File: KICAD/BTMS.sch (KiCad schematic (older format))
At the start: 314 parts, among them J1 fan, J10 U1COMMS, J11 U2COMMS, J13 IntBTemp, J14 ctrlTemp, J15 12Vout, J16 12Vin, J17 5Vout, J2 mContactor, J3 Tac, J5 ICSP, J7 5Vout, J9 key, Q1 PSMN5R6-100BS, Q10 PSMN5R6-100BS, Q11 DMN65D8L, Q12 DMN65D8L, Q13 FDN340P, Q14 ZXTP2025FTA, Q15 ZXTP2025FTA, Q16 ZXTP2025FTA, Q18 DMN65D8L, Q2 PSMN5R6-100BS, Q3 PSMN5R6-100BS, Q4 DMN65D8L, Q5 DMN65D8L, Q6 DMN65D8L, Q7 DMN65D8L, Q8 PSMN5R6-100BS, Q9 FDN340P, U1 R-78HB12-0.5, U10 A41AS12VDC, U11 A41AS12VDC, U12 A41AS12VDC, U13 A41AS12VDC, U14 A41AS12VDC, U15 NL17SZ74USG, U2 ACS780xLRTR-050B, U3 UCC27201DDAR, U4 FAN3111ESX, U5 HCPL-3120, U6 L7805CV, U7 LTV-817S, U8 dsPIC30F3011-PT, U9 LM62CIM3/NOPB

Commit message: Updated KICAD custom parts.
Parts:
- U10, U11, U12, U13, U14: symbol a4series:A4series -> BTMS-rescue:A4series-a4series
- U15: symbol nl17sz74usg:NL17SZ74USG -> BTMS-rescue:NL17SZ74USG-nl17sz74usg
- U3: symbol ir2104power:IR2104Power -> BTMS-rescue:IR2104Power-ir2104power
- U8: symbol dspic:dsPIC30F3011-PT -> BTMS-rescue:dsPIC30F3011-PT-dspic
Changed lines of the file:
@@
 Connection ~ 1400 3100
 $Comp
-L ir2104power:IR2104Power U3
+L BTMS-rescue:IR2104Power-ir2104power U3
 U 1 1 5EB473C3
 P 4100 5700
@@
 Connection ~ 13400 8800
 $Comp
-L dspic:dsPIC30F3011-PT U8
+L BTMS-rescue:dsPIC30F3011-PT-dspic U8
 U 1 1 5E12A7C4
 P 13550 7500
@@
 	1650 5400 1650 5750
 $Comp
-L a4series:A4series U10
+L BTMS-rescue:A4series-a4series U10
 U 1 1 5FB8A273
 P 2100 8350
@@
 $EndComp
 $Comp
-L a4series:A4series U11
+L BTMS-rescue:A4series-a4series U11
 U 1 1 5FB8C6D2
 P 2100 9500
@@
 $EndComp
 $Comp
-L a4series:A4series U12
+L BTMS-rescue:A4series-a4series U12
 U 1 1 5FB8DA7B
 P 2100 10700
@@
 $EndComp
 $Comp
-L a4series:A4series U14
+L BTMS-rescue:A4series-a4series U14
 U 1 1 5FB8F1EB
 P 5050 10150
@@
 Connection ~ 5200 9700
 $Comp
-L a4series:A4series U13
+L BTMS-rescue:A4series-a4series U13
 U 1 1 5FB905AA
 P 5050 8600
@@
 	5250 6850 5350 6850
 $Comp
-L nl17sz74usg:NL17SZ74USG U15
+L BTMS-rescue:NL17SZ74USG-nl17sz74usg U15
 U 1 1 6056CB7B
 P 5500 5800

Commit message: Updated parts list. Updated Gerber files. Updated board to reflect schematic. Tweaked some parts of the schematic.
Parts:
- C110, C13, C15, C16, C17, C18, C19, C2, C20, C21, C22, C23, C36, C65, C75, C76, C8: DK_Detail_Page (none) -> https://www.digikey.com/en/products/detail/panasonic-electr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; Digi-Key_PN (none) -> PCF1126CT-ND
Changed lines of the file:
@@
 F 2 "Capacitors_SMD:C_0603" H 5038 3800 50  0001 C CNN
 F 3 "~" H 5000 3950 50  0001 C CNN
-F 4 "" H 5000 3950 50  0001 C CNN "DK_Detail_Page"
-F 5 "" H 5000 3950 50  0001 C CNN "Digi-Key_PN"
+F 4 "https://www.digikey.com/en/products/detail/panasonic-electronic-components/ECP-U1C104MA5/285446?s=N4IgTCBcDaIIxzANgCIGkBKBaAcikAugL5A" H 5000 3950 50  0001 C CNN "DK_Detail_Page"
+F 5 "PCF1126CT-ND" H 5000 3950 50  0001 C CNN "Digi-Key_PN"
 	1    5000 3950
 	1    0    0    -1
@@
 F 2 "Capacitors_SMD:C_0603" H 12638 5900 50  0001 C CNN
 F 3 "~" H 12600 6050 50  0001 C CNN
-F 4 "" H 12600 6050 50  0001 C CNN "DK_Detail_Page"
-F 5 "" H 12600 6050 50  0001 C CNN "Digi-Key_PN"
+F 4 "https://www.digikey.com/en/products/detail/panasonic-electronic-components/ECP-U1C104MA5/285446?s=N4IgTCBcDaIIxzANgCIGkBKBaAcikAugL5A" H 12600 6050 50  0001 C CNN "DK_Detail_Page"
+F 5 "PCF1126CT-ND" H 12600 6050 50  0001 C CNN "Digi-Key_PN"
 	1    12600 6050
 	1    0    0    -1
@@
 F 2 "Capacitors_SMD:C_0603" H 12888 5900 50  0001 C CNN
 F 3 "~" H 12850 6050 50  0001 C CNN
-F 4 "" H 12850 6050 50  0001 C CNN "DK_Detail_Page"
-F 5 "" H 12850 6050 50  0001 C CNN "Digi-Key_PN"
+F 4 "https://www.digikey.com/en/products/detail/panasonic-electronic-components/ECP-U1C104MA5/285446?s=N4IgTCBcDaIIxzANgCIGkBKBaAcikAugL5A" H 12850 6050 50  0001 C CNN "DK_Detail_Page"
+F 5 "PCF1126CT-ND" H 12850 6050 50  0001 C CNN "Digi-Key_PN"
 	1    12850 6050
 	1    0    0    -1
@@
 F 2 "Capacitors_SMD:C_0603" H 12388 5900 50  0001 C CNN
 F 3 "~" H 12350 6050 50  0001 C CNN
-F 4 "" H 12350 6050 50  0001 C CNN "DK_Detail_Page"
-F 5 "" H 12350 6050 50  0001 C CNN "Digi-Key_PN"
+F 4 "https://www.digikey.com/en/products/detail/panasonic-electronic-components/ECP-U1C104MA5/285446?s=N4IgTCBcDaIIxzANgCIGkBKBaAcikAugL5A" H 12350 6050 50  0001 C CNN "DK_Detail_Page"
+F 5 "PCF1126CT-ND" H 12350 6050 50  0001 C CNN "Digi-Key_PN"
 	1    12350 6050
 	1    0    0    -1
@@
 F 2 "Capacitors_SMD:C_0603" H 12138 5900 50  0001 C CNN
 F 3 "~" H 12100 6050 50  0001 C CNN
-F 4 "" H 12100 6050 50  0001 C CNN "DK_Detail_Page"
-F 5 "" H 12100 6050 50  0001 C CNN "Digi-Key_PN"
+F 4 "https://www.digikey.com/en/products/detail/panasonic-electronic-components/ECP-U1C104MA5/285446?s=N4IgTCBcDaIIxzANgCIGkBKBaAcikAugL5A" H 12100 6050 50  0001 C CNN "DK_Detail_Page"
+F 5 "PCF1126CT-ND" H 12100 6050 50  0001 C CNN "Digi-Key_PN"
 	1    12100 6050
 	1    0    0    -1
@@
 F 2 "Capacitors_SMD:C_0603" H 11088 8150 50  0001 C CNN
 F 3 "~" H 11050 8300 50  0001 C CNN
-F 4 "" H 11050 8300 50  0001 C CNN "DK_Detail_Page"
-F 5 "" H 11050 8300 50  0001 C CNN "Digi-Key_PN"
+F 4 "https://www.digikey.com/en/products/detail/panasonic-electronic-components/ECP-U1C104MA5/285446?s=N4IgTCBcDaIIxzANgCIGkBKBaAcikAugL5A" H 11050 8300 50  0001 C CNN "DK_Detail_Page"
+F 5 "PCF1126CT-ND" H 11050 8300 50  0001 C CNN "Digi-Key_PN"
 	1    11050 8300
 	1    0    0    -1
@@
 F 2 "Capacitors_SMD:C_0603" H 10588 1550 50  0001 C CNN
 F 3 "~" H 10550 1700 50  0001 C CNN
-F 4 "" H 10550 1700 50  0001 C CNN "DK_Detail_Page"
-F 5 "" H 10550 1700 50  0001 C CNN "Digi-Key_PN"
+F 4 "https://www.digikey.com/en/products/detail/panasonic-electronic-components/ECP-U1C104MA5/285446?s=N4IgTCBcDaIIxzANgCIGkBKBaAcikAugL5A" H 10550 1700 50  0001 C CNN "DK_Detail_Page"
+F 5 "PCF1126CT-ND" H 10550 1700 50  0001 C CNN "Digi-Key_PN"
 	1    10550 1700
 	1    0    0    -1
@@
 F 2 "Capacitors_SMD:C_0603" H 10588 2250 50  0001 C CNN
 F 3 "~" H 10550 2400 50  0001 C CNN
-F 4 "" H 10550 2400 50  0001 C CNN "DK_Detail_Page"
-F 5 "" H 10550 2400 50  0001 C CNN "Digi-Key_PN"
+F 4 "https://www.digikey.com/en/products/detail/panasonic-electronic-components/ECP-U1C104MA5/285446?s=N4IgTCBcDaIIxzANgCIGkBKBaAcikAugL5A" H 10550 2400 50  0001 C CNN "DK_Detail_Page"
+F 5 "PCF1126CT-ND" H 10550 2400 50  0001 C CNN "Digi-Key_PN"
 	1    10550 2400
 	1    0    0    -1
@@
 F 2 "Capacitors_SMD:C_0603" H 7638 1700 50  0001 C CNN
 F 3 "~" H 7600 1850 50  0001 C CNN
-F 4 "" H 7600 1850 50  0001 C CNN "DK_Detail_Page"
-F 5 "" H 7600 1850 50  0001 C CNN "Digi-Key_PN"
+F 4 "https://www.digikey.com/en/products/detail/panasonic-electronic-components/ECP-U1C104MA5/285446?s=N4IgTCBcDaIIxzANgCIGkBKBaAcikAugL5A" H 7600 1850 50  0001 C CNN "DK_Detail_Page"
+F 5 "PCF1126CT-ND" H 7600 1850 50  0001 C CNN "Digi-Key_PN"
 	1    7600 1850
 	1    0    0    -1
@@
 F 2 "Capacitors_SMD:C_0603" H 8288 1700 50  0001 C CNN
 F 3 "~" H 8250 1850 50  0001 C CNN
-F 4 "" H 8250 1850 50  0001 C CNN "DK_Detail_Page"
-F 5 "" H 8250 1850 50  0001 C CNN "Digi-Key_PN"
+F 4 "https://www.digikey.com/en/products/detail/panasonic-electronic-components/ECP-U1C104MA5/285446?s=N4IgTCBcDaIIxzANgCIGkBKBaAcikAugL5A" H 8250 1850 50  0001 C CNN "DK_Detail_Page"
+F 5 "PCF1126CT-ND" H 8250 1850 50  0001 C CNN "Digi-Key_PN"
 	1    8250 1850
 	1    0    0    -1
@@
 F 2 "Capacitors_SMD:C_0603" H 10488 3150 50  0001 C CNN
 F 3 "~" H 10450 3300 50  0001 C CNN
-F 4 "" H 10450 3300 50  0001 C CNN "DK_Detail_Page"
-F 5 "" H 10450 3300 50  0001 C CNN "Digi-Key_PN"
+F 4 "https://www.digikey.com/en/products/detail/panasonic-electronic-components/ECP-U1C104MA5/285446?s=N4IgTCBcDaIIxzANgCIGkBKBaAcikAugL5A" H 10450 3300 50  0001 C CNN "DK_Detail_Page"
+F 5 "PCF1126CT-ND" H 10450 3300 50  0001 C CNN "Digi-Key_PN"
 	1    10450 3300
 	1    0    0    -1
@@
 F 2 "Capacitors_SMD:C_0603" H 10688 1050 50  0001 C CNN
 F 3 "~" H 10650 1200 50  0001 C CNN
-F 4 "" H 10650 1200 50  0001 C CNN "DK_Detail_Page"
-F 5 "" H 10650 1200 50  0001 C CNN "Digi-Key_PN"
+F 4 "https://www.digikey.com/en/products/detail/panasonic-electronic-components/ECP-U1C104MA5/285446?s=N4IgTCBcDaIIxzANgCIGkBKBaAcikAugL5A" H 10650 1200 50  0001 C CNN "DK_Detail_Page"
+F 5 "PCF1126CT-ND" H 10650 1200 50  0001 C CNN "Digi-Key_PN"
 	1    10650 1200
 	1    0    0    -1
@@
 F 2 "Capacitors_SMD:C_0603" H 6838 1050 50  0001 C CNN
 F 3 "~" H 6800 1200 50  0001 C CNN
-F 4 "" H 6800 1200 50  0001 C CNN "DK_Detail_Page"
-F 5 "" H 6800 1200 50  0001 C CNN "Digi-Key_PN"
+F 4 "https://www.digikey.com/en/products/detail/panasonic-electronic-components/ECP-U1C104MA5/285446?s=N4IgTCBcDaIIxzANgCIGkBKBaAcikAugL5A" H 6800 1200 50  0001 C CNN "DK_Detail_Page"
+F 5 "PCF1126CT-ND" H 6800 1200 50  0001 C CNN "Digi-Key_PN"
 	1    6800 1200
 	1    0    0    -1
@@
 F 2 "Capacitors_SMD:C_0603" H 5788 4800 50  0001 C CNN
 F 3 "~" H 5750 4950 50  0001 C CNN
-F 4 "" H 5750 4950 50  0001 C CNN "DK_Detail_Page"
-F 5 "" H 5750 4950 50  0001 C CNN "Digi-Key_PN"
+F 4 "https://www.digikey.com/en/products/detail/panasonic-electronic-components/ECP-U1C104MA5/285446?s=N4IgTCBcDaIIxzANgCIGkBKBaAcikAugL5A" H 5750 4950 50  0001 C CNN "DK_Detail_Page"
+F 5 "PCF1126CT-ND" H 5750 4950 50  0001 C CNN "Digi-Key_PN"
 	1    5750 4950
 	1    0    0    -1
@@
 F 2 "Capacitors_SMD:C_0603" H 4588 4800 50  0001 C CNN
 F 3 "~" H 4550 4950 50  0001 C CNN
-F 4 "" H 4550 4950 50  0001 C CNN "DK_Detail_Page"
-F 5 "" H 4550 4950 50  0001 C CNN "Digi-Key_PN"
+F 4 "https://www.digikey.com/en/products/detail/panasonic-electronic-components/ECP-U1C104MA5/285446?s=N4IgTCBcDaIIxzANgCIGkBKBaAcikAugL5A" H 4550 4950 50  0001 C CNN "DK_Detail_Page"
+F 5 "PCF1126CT-ND" H 4550 4950 50  0001 C CNN "Digi-Key_PN"
 	1    4550 4950
 	1    0    0    -1
@@
 F 2 "Capacitors_SMD:C_0603" H 2788 6500 50  0001 C CNN
 F 3 "~" H 2750 6650 50  0001 C CNN
-F 4 "" H 2750 6650 50  0001 C CNN "DK_Detail_Page"
-F 5 "" H 2750 6650 50  0001 C CNN "Digi-Key_PN"
+F 4 "https://www.digikey.com/en/products/detail/panasonic-electronic-components/ECP-U1C104MA5/285446?s=N4IgTCBcDaIIxzANgCIGkBKBaAcikAugL5A" H 2750 6650 50  0001 C CNN "DK_Detail_Page"
+F 5 "PCF1126CT-ND" H 2750 6650 50  0001 C CNN "Digi-Key_PN"
 	1    2750 6650
 	1    0    0    -1
@@
 F 2 "Capacitors_SMD:C_0603" H 6338 6000 50  0001 C CNN
 F 3 "~" H 6300 6150 50  0001 C CNN
-F 4 "" H 6300 6150 50  0001 C CNN "DK_Detail_Page"
-F 5 "" H 6300 6150 50  0001 C CNN "Digi-Key_PN"
+F 4 "https://www.digikey.com/en/products/detail/panasonic-electronic-components/ECP-U1C104MA5/285446?s=N4IgTCBcDaIIxzANgCIGkBKBaAcikAugL5A" H 6300 6150 50  0001 C CNN "DK_Detail_Page"
+F 5 "PCF1126CT-ND" H 6300 6150 50  0001 C CNN "Digi-Key_PN"
 	1    6300 6150
 	1    0    0    -1

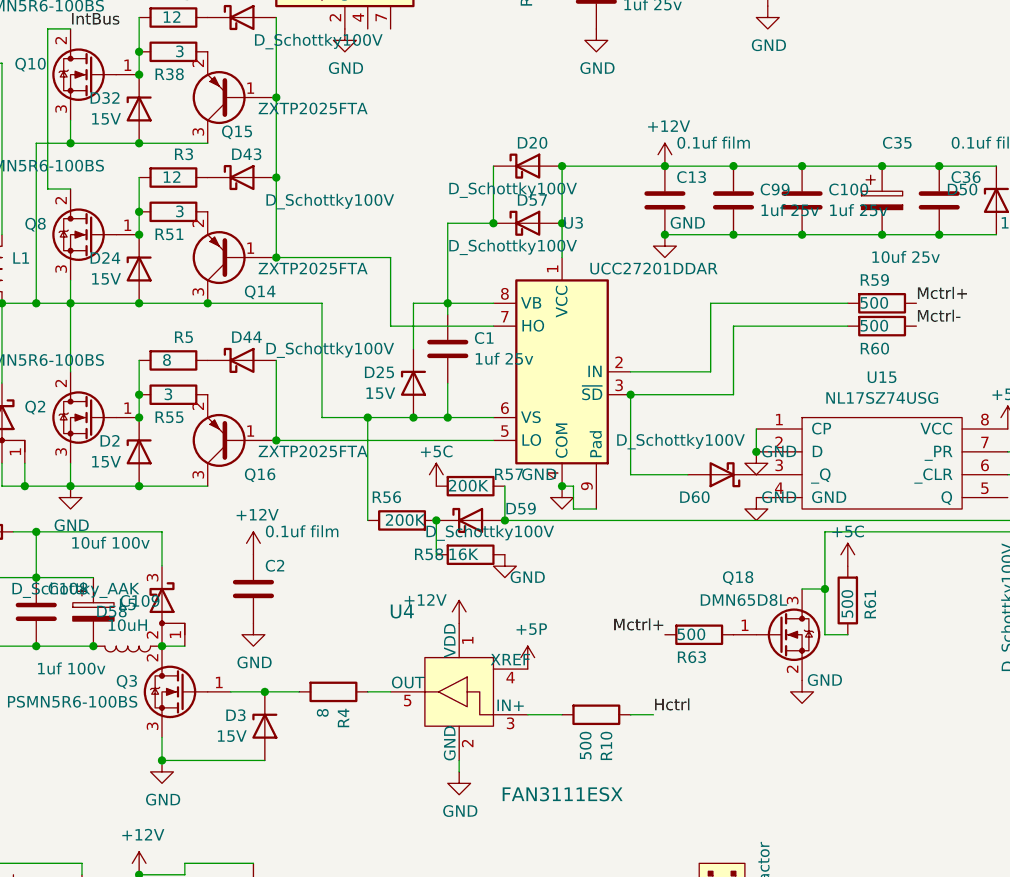
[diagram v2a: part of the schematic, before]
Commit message: Updated U3 to reflect proper pinout for UCC27201DDAR
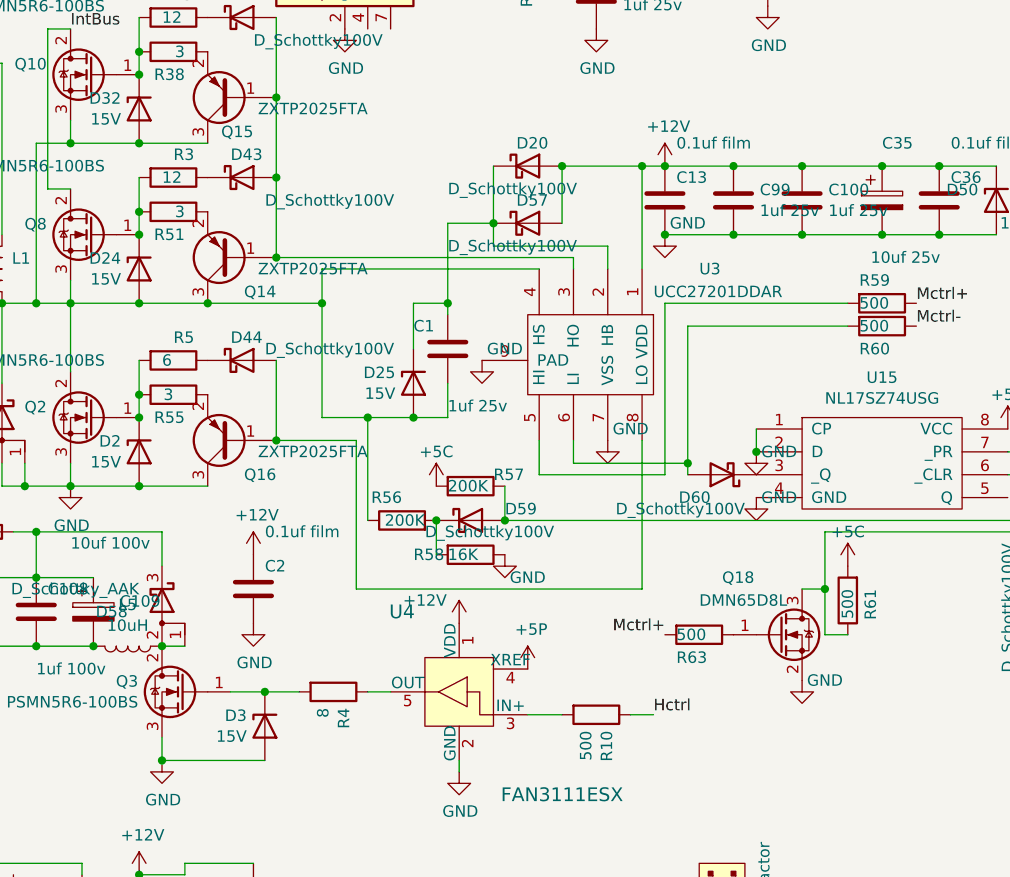
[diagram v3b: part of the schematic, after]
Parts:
- removed U3: UCC27201DDAR, Housings_SOIC:TI_SO-PowerPAD-8_ThermalVias, symbol BTMS-rescue:IR2104Power-ir2104power
- added U3: UCC27201DDAR, Housings_SOIC:TI_SO-PowerPAD-8_ThermalVias, symbol ucc27201ddar:UCC27201DDAR
- R5: value 8 -> 6
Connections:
- net +12V: now also U3.1 (VDD)
- net GND: now also U3.7 (VSS), U3.9 (PAD)
- net at C1.2, D24.2 (A), D25.2 (A)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: now also U3.4 (HS)
- net at R59.2: now also U3.5 (HI)
- net at D60.2 (A), R60.2: now also U3.6 (LI)
- net at D44.2 (A), Q16.1 (B): now also U3.8 (LO)
- net at D42.2 (A), D43.2 (A), Q14.1 (B)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: now also U3.3 (HO)
- net at C1.1, D20.1 (K), D25.1 (K)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: now also U3.2 (HB)
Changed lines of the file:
@@
 Wire Wire Line
 	3950 7200 4100 7200
-Wire Wire Line
-	4500 7200 4400 7200
 $Comp
 L dk_PMIC-Gate-Drivers:FAN3111ESX U4
@@
 U 1 1 5EE1AACE
 P 3600 5600
-F 0 "C1" H 3715 5646 50  0000 L CNN
-F 1 "1uf 25v" H 3715 5555 50  0000 L CNN
+F 0 "C1" H 3450 5700 50  0000 L CNN
+F 1 "1uf 25v" H 3600 5350 50  0000 L CNN
 F 2 "Capacitors_SMD:C_0603" H 3638 5450 50  0001 C CNN
 F 3 "~" H 3600 5600 50  0001 C CNN
@@
 P 2400 5650
 F 0 "R5" V 2300 5650 50  0000 L CNN
-F 1 "8" V 2400 5600 50  0000 L CNN
+F 1 "6" V 2400 5600 50  0000 L CNN
 F 2 "Resistors_SMD:R_0603" V 2330 5650 50  0001 C CNN
 F 3 "~" H 2400 5650 50  0001 C CNN
@@
 	1700 3100 1400 3100
 Connection ~ 1400 3100
-$Comp
-L BTMS-rescue:IR2104Power-ir2104power U3
-U 1 1 5EB473C3
-P 4100 5700
-F 0 "U3" H 4050 6350 50  0000 C CNN
-F 1 "UCC27201DDAR" H 3700 6150 50  0000 C CNN
-F 2 "Housings_SOIC:TI_SO-PowerPAD-8_ThermalVias" H 4100 5700 50  0001 C CIN
-F 3 "https://www.infineon.com/dgdl/ir2104.pdf?fileId=5546d462533600a4015355c7c1c31671" H 4100 5700 50  0001 C CNN
-F 4 "https://www.digikey.com/en/products/detail/texas-instruments/UCC27201DDAR/1911333" H 4100 5700 50  0001 C CNN "DK_Detail_Page"
-F 5 "296-31998-1-ND" H 4100 5700 50  0001 C CNN "Digi-Key_PN"
-	1    4100 5700
-	-1   0    0    -1
-$EndComp
 Wire Wire Line
 	3600 5400 3600 5450
@@
 	3600 5750 3600 5900
 Wire Wire Line
-	3600 5900 3800 5900
-Wire Wire Line
 	3600 5900 3450 5900
-Connection ~ 3600 5900
 $Comp
 L power:GND #PWR015
 U 1 1 5ECF520D
-P 4100 6200
-F 0 "#PWR015" H 4100 5950 50  0001 C CNN
-F 1 "GND" H 4000 6250 50  0000 C CNN
-F 2 "" H 4100 6200 50  0001 C CNN
-F 3 "" H 4100 6200 50  0001 C CNN
-	1    4100 6200
+P 3750 5650
+F 0 "#PWR015" H 3750 5400 50  0001 C CNN
+F 1 "GND" H 3850 5700 50  0000 C CNN
+F 2 "" H 3750 5650 50  0001 C CNN
+F 3 "" H 3750 5650 50  0001 C CNN
+	1    3750 5650
 	1    0    0    -1
 $EndComp
@@
 $EndComp
 Wire Wire Line
-	4550 4800 4100 4800
+	4550 4800 4450 4800
 Connection ~ 4550 4800
 $Comp
@@
 Connection ~ 2450 650
 Connection ~ 3300 600
-Wire Wire Line
-	4250 6300 4150 6300
-Wire Wire Line
-	4150 6300 4150 6200
-Wire Wire Line
-	4150 6200 4100 6200
-Connection ~ 4100 6200
 $Comp
 L Device:R R51
@@
 	0    -1   -1   0
 $EndComp
-Wire Wire Line
-	3800 5400 3600 5400
 Connection ~ 3600 5400
 Wire Wire Line
@@
 Wire Wire Line
 	3450 5400 3600 5400
-Wire Wire Line
-	3800 5500 3350 5500
 $Comp
 L Device:Q_PNP_BEC Q14
@@
 Wire Wire Line
 	2850 4850 2850 5200
-Wire Wire Line
-	2850 5200 3350 5200
-Wire Wire Line
-	3350 5200 3350 5500
 Connection ~ 2850 5200
 Wire Wire Line
@@
 	2850 5650 2850 6000
 Wire Wire Line
-	2850 6000 3800 6000
-Connection ~ 2850 6000
-Wire Wire Line
 	3450 5900 3250 5900
 Wire Wire Line
@@
 	1    0    0    -1
 $EndComp
-Connection ~ 4100 5050
-Wire Wire Line
-	4100 5050 4100 5200
 Wire Wire Line
 	3600 5050 3800 5050
@@
 $EndComp
 Wire Wire Line
-	5350 5500 4850 5500
-Wire Wire Line
-	5350 5400 4750 5400
-Wire Wire Line
-	4750 5400 4750 5700
-Wire Wire Line
-	4750 5700 4400 5700
-Wire Wire Line
-	4400 6150 4650 6150
-Wire Wire Line
-	4400 5800 4400 6150
-Wire Wire Line
-	4400 5800 4850 5800
-Wire Wire Line
-	4850 5500 4850 5800
-Connection ~ 4400 5800
-Wire Wire Line
 	5250 6400 6100 6400
 Wire Wire Line
@@
 P 4800 6150
 F 0 "D60" H 4850 6250 50  0000 L CNN
-F 1 "D_Schottky100V" H 4700 6000 50  0000 L CNN
+F 1 "D_Schottky100V" H 4700 6300 50  0000 L CNN
 F 2 "Diodes_SMD:D_SOD-123" H 4800 6150 50  0001 C CNN
 F 3 "~" H 4800 6150 50  0001 C CNN
@@
 	6200 9950 6000 9950
 Connection ~ 6000 9950
+$Comp
+L ucc27201ddar:UCC27201DDAR U3
+U 1 1 61187C6B
+P 4350 5600
+F 0 "U3" V 4000 5950 50  0000 L CNN
+F 1 "UCC27201DDAR" V 4100 5750 50  0000 L CNN
+F 2 "Housings_SOIC:TI_SO-PowerPAD-8_ThermalVias" H 4350 5600 50  0001 C CNN
+F 3 "https://www.ti.com/lit/ds/symlink/ucc27200.pdf?HQS=dis-dk-null-digikeymode-dsf-pf-null-wwe&ts=1628373640405&ref_url=https%253A%252F%252Fwww.ti.com%252Fgeneral%252Fdocs%252Fsuppproductinfo.tsp%253FdistId%253D10%2526gotoUrl%253Dhttps%253A%252F%252Fwww.ti.com%252Flit%252Fgpn%252Fucc27200" H 4350 5600 50  0001 C CNN
+F 4 "https://www.digikey.com/en/products/detail/texas-instruments/UCC27201DDAR/1911333" H 4350 5600 50  0001 C CNN "DK_Detail_Page"
+F 5 "296-31998-1-ND" H 4350 5600 50  0001 C CNN "Digi-Key_PN"
+	1    4350 5600
+	0    1    1    0
+$EndComp
+Wire Wire Line
+	4450 5250 4450 4800
+Wire Wire Line
+	4400 7200 4500 7200
+Connection ~ 4450 4800
+Wire Wire Line
+	4450 4800 4100 4800
+Wire Wire Line
+	4300 5250 4300 5150
+Wire Wire Line
+	4300 5150 3800 5150
+Wire Wire Line
+	3800 5150 3800 5050
+Wire Wire Line
+	4150 5250 4150 5200
+Wire Wire Line
+	2850 5200 4150 5200
+Wire Wire Line
+	4000 5250 3050 5250
+Wire Wire Line
+	3050 5250 3050 5400
+Connection ~ 3050 5400
+Wire Wire Line
+	2850 6000 3200 6000
+Wire Wire Line
+	3200 6000 3200 6650
+Wire Wire Line
+	3200 6650 4450 6650
+Wire Wire Line
+	4450 6650 4450 6000
+Connection ~ 2850 6000
+$Comp
+L power:GND #PWR0153
+U 1 1 6142815F
+P 4300 6000
+F 0 "#PWR0153" H 4300 5750 50  0001 C CNN
+F 1 "GND" H 4400 6050 50  0000 C CNN
+F 2 "" H 4300 6000 50  0001 C CNN
+F 3 "" H 4300 6000 50  0001 C CNN
+	1    4300 6000
+	1    0    0    -1
+$EndComp
+Wire Wire Line
+	4150 6000 4150 6100
+Wire Wire Line
+	4150 6100 4650 6100
+Wire Wire Line
+	4650 6100 4650 5500
+Wire Wire Line
+	4650 5500 5350 5500
+Wire Wire Line
+	4550 5400 4550 6150
+Wire Wire Line
+	4550 6150 4000 6150
+Wire Wire Line
+	4000 6150 4000 6000
+Wire Wire Line
+	4550 5400 5350 5400
+Wire Wire Line
+	4650 6150 4650 6100
+Connection ~ 4650 6100
 $EndSCHEMATC
